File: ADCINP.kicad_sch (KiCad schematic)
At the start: 23 parts

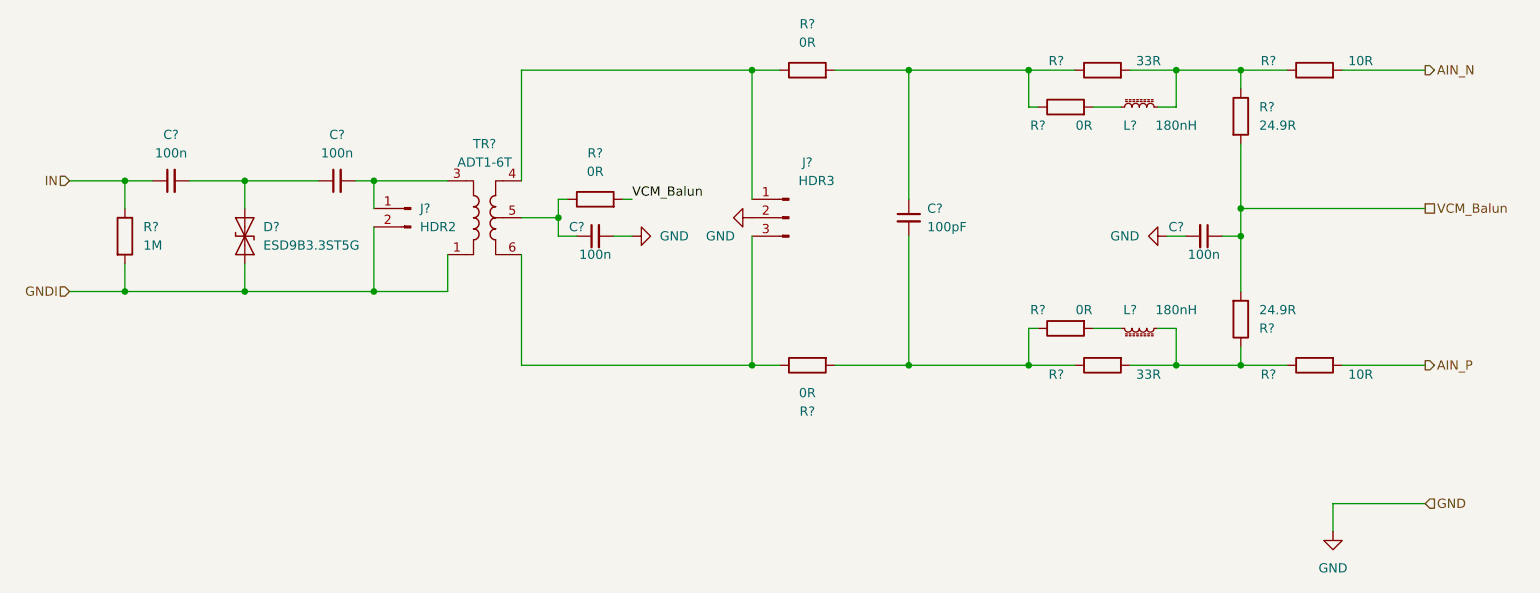
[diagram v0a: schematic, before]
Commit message: annotated and packages defined
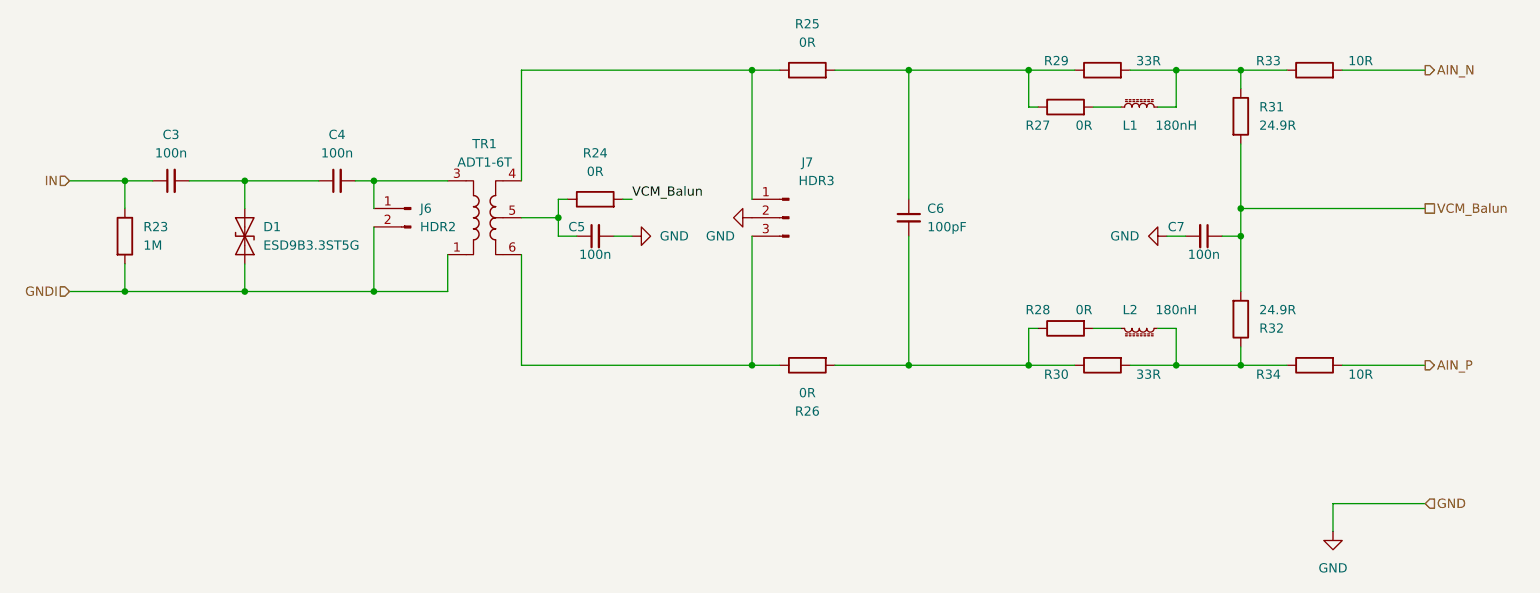
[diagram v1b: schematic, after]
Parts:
- C3, C4, C5, C6, C7: renamed from C?; footprint (none) -> Capacitor_SMD:C_0805_2012Metric
- J6: renamed from J?; footprint (none) -> Connector_PinHeader_2.54mm:PinHeader_1x02_P2.54mm_Vertical
- J7: renamed from J?; footprint (none) -> Connector_PinHeader_2.54mm:PinHeader_1x03_P2.54mm_Vertical
- L1, L2: renamed from L?; footprint (none) -> Resistor_SMD:R_0805_2012Metric
- R23, R24, R25, R26, R27, R28, R29, R30, R31, R32, R33, R34: renamed from R?; footprint (none) -> Resistor_SMD:R_0805_2012Metric
- gave numbers to parts that had none: 2
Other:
- company: (none) -> papamidas DM1CR
- title: (none) -> H7DDCADC
